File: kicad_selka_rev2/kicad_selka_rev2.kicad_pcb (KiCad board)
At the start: 2 copper layers, 89.2 x 194.1 mm, 88 parts, among them J1 Conn_01x02, J2 Conn_01x06, J3 Conn_01x08, J4 Conn_01x08, SW1 PUSH, U1 ATtiny861A SOIC20

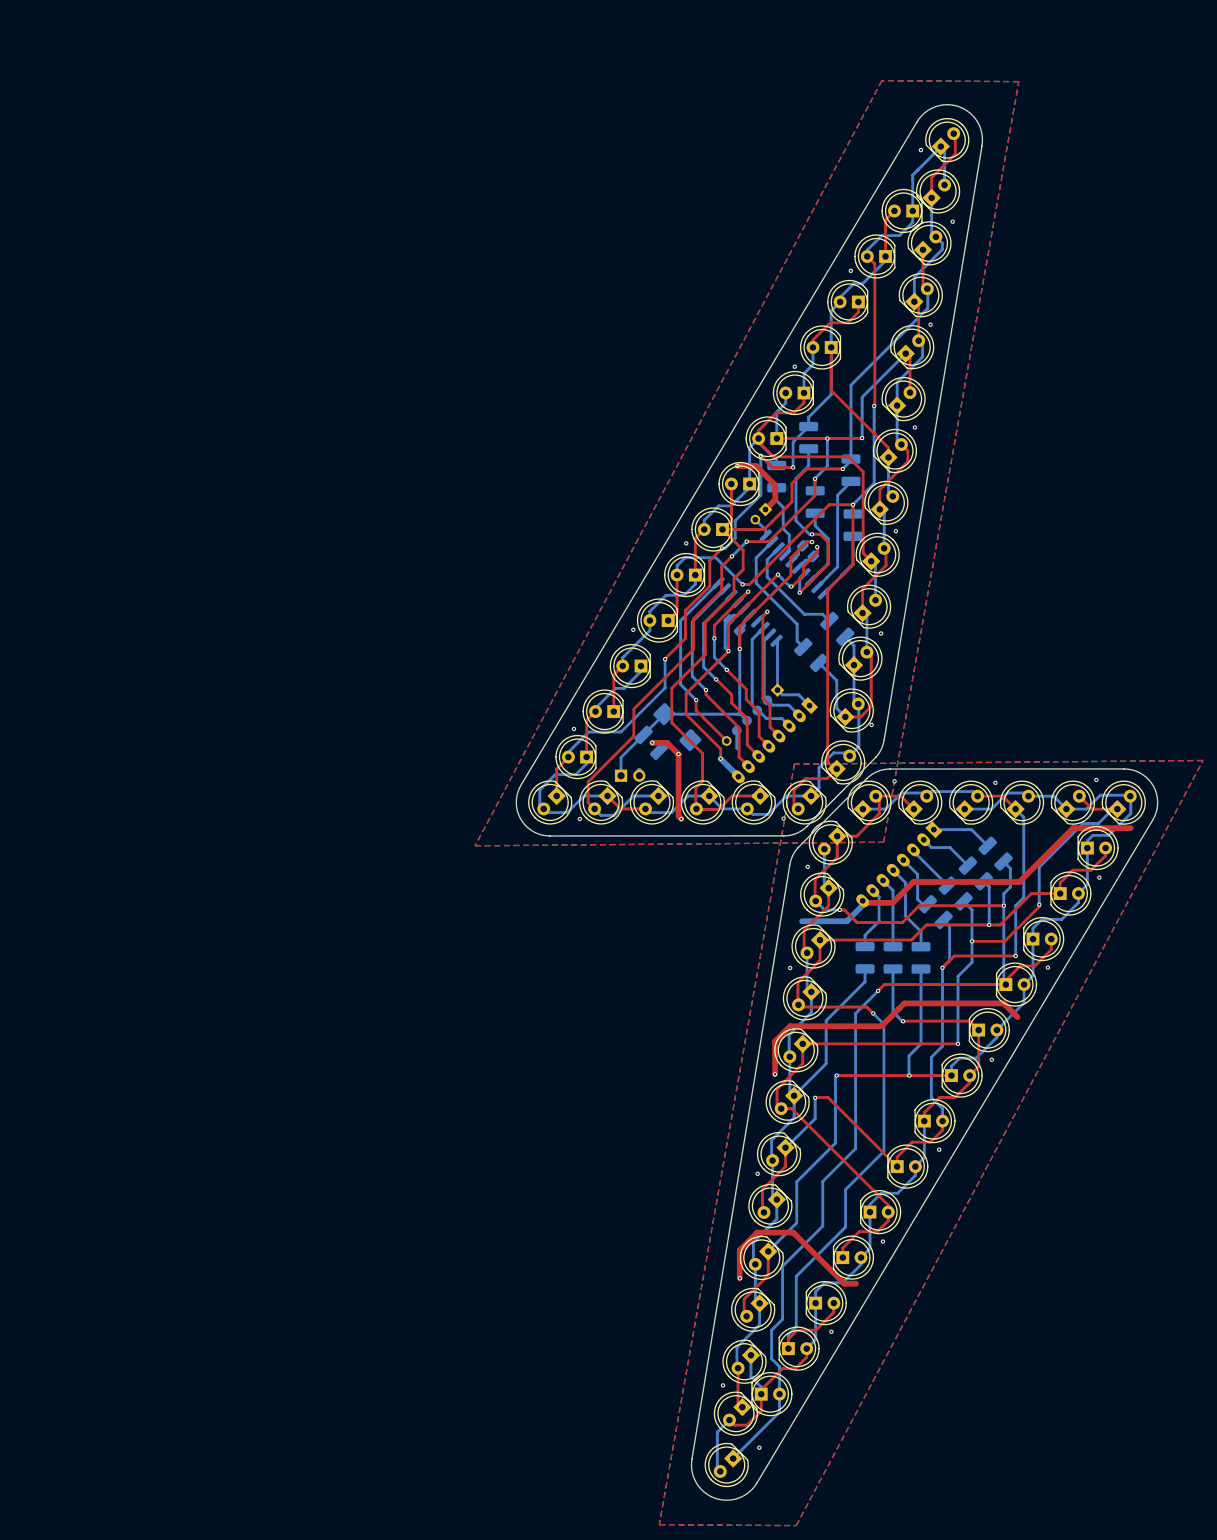
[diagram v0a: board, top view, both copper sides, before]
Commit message: Selkäsalama rev2 done
Skema ja leiska valmis rev2.
Tilattu R2-260625. Toimii ja näyttää hjuvalta.

Siirtin kamaa /archive kansioon. mm. vanhat ja proto versiot.
Vanhat media tiedostot jne.
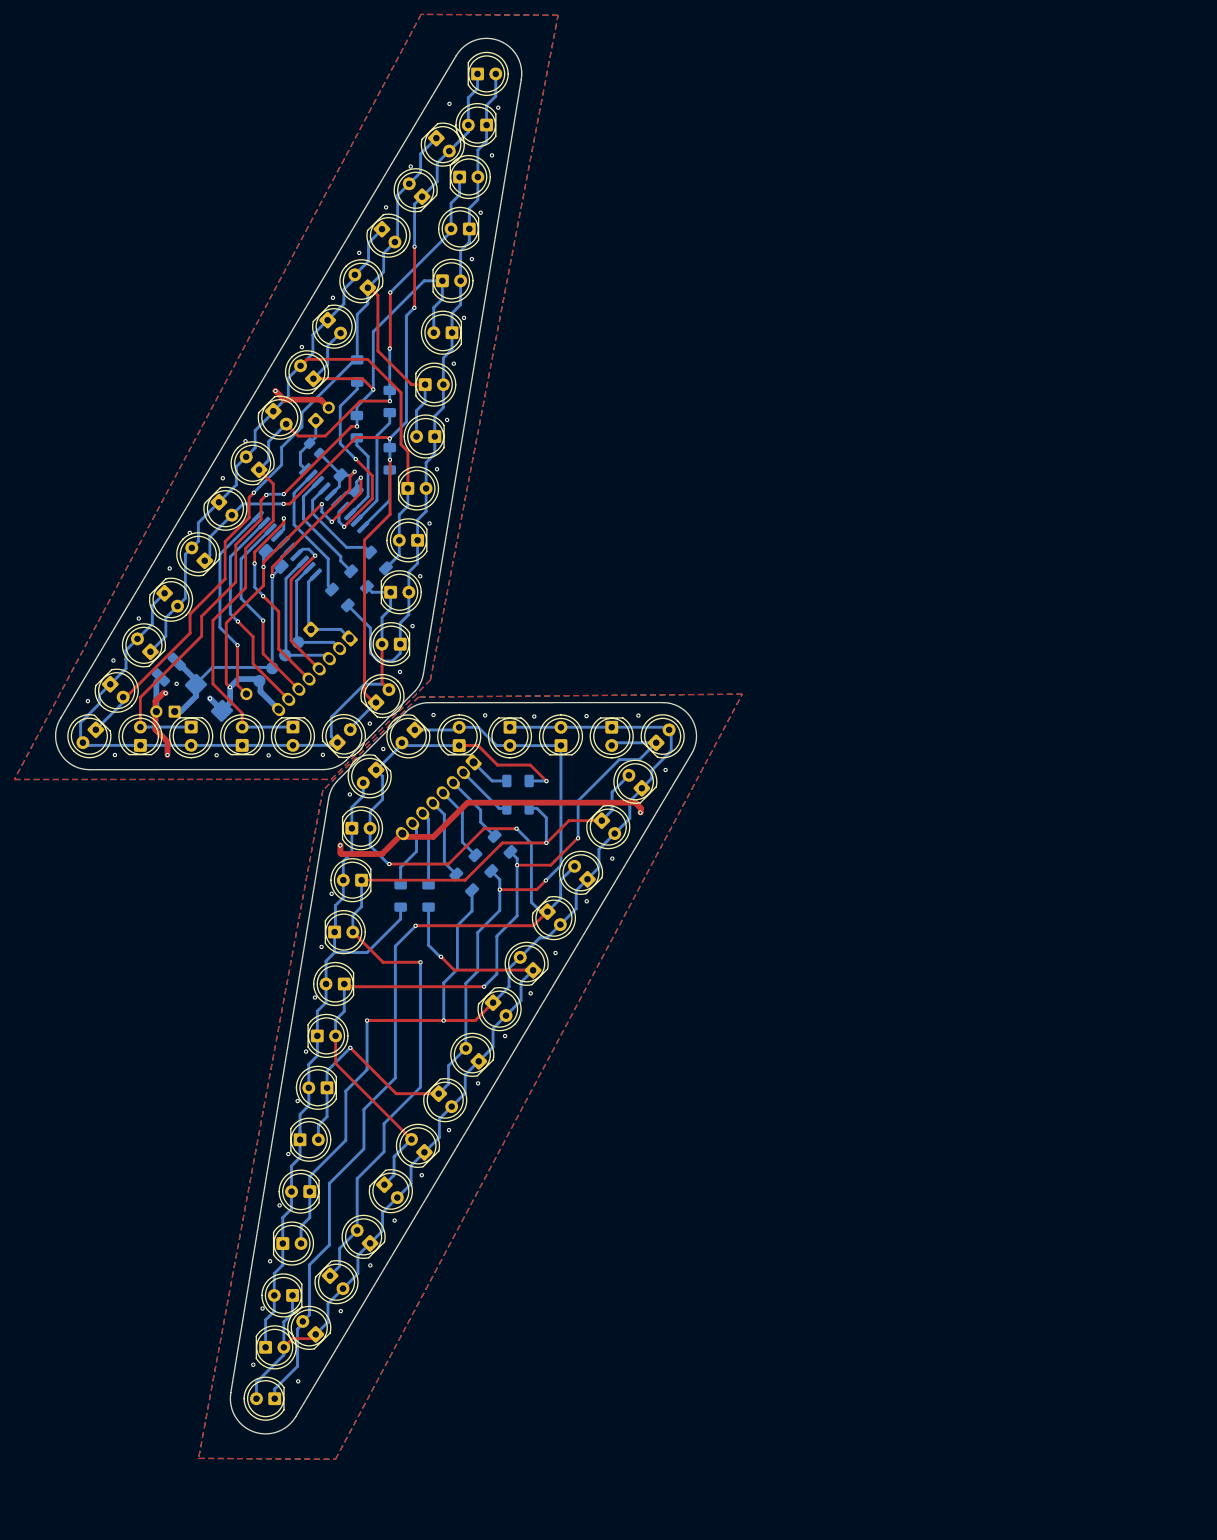
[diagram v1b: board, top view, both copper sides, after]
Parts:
- added G***: LOGO, footprintteja:pesu, B.Cu at (68.7, 162.2)
- added G***: LOGO, footprintteja:avr_logo, B.Cu at (69.1, 64.0)
- added R16: 4.7K, Resistor_SMD:R_0805_2012Metric_Pad1.20x1.40mm_HandSolder, B.Cu at (57.8, 80.9)
- C2, C3: footprint Capacitor_SMD:C_0805_2012Metric_Pad1.18x1.45mm_HandSolder -> Capacitor_SMD:C_1206_3216Metric_Pad1.33x1.80mm_HandSolder
- D1, D10, D11, D12, D13, D14, D15, D16, D17, D18, D19, D2, D20, D21, D22, D23, D24, D25, D26, D27, D28, D29, D3, D30, D31, D32, D33, D34, D35, D36, D37, D38, D39, D4, D40, D41, D42, D43, D44, D45, D46, D47, D48, D49, D5, D50, D51, D52, D53, D54, D55, D56, D57, D58, D59, D6, D60, D61, D62, D63, D64, D7, D8, D9: footprint Library_zani:LED_D5.0mm_blue_zani -> footprintteja:LED_D5.0mm_blue_zani
- J2: footprint footprintteja:PinHeader_1x06_P2.00mm_Horizontal_smd_tht -> footprintteja:PinHeader_1x06_P2.54mm_Horizontal_smd_tht
- R1, R10, R11, R12, R13, R14, R2, R3, R4, R5, R6, R7, R8, R9: value 50 -> 27; footprint Resistor_SMD:R_1210_3225Metric_Pad1.30x2.65mm_HandSolder -> Resistor_SMD:R_1206_3216Metric_Pad1.30x1.75mm_HandSolder
- SW1: value PUSH -> LIUKU; footprint Connector_PinHeader_2.00mm:PinHeader_1x02_P2.00mm_Vertical -> Connector_PinHeader_2.54mm:PinHeader_1x02_P2.54mm_Vertical
- U1: value ATtiny861A SOIC20 -> ATtiny 861A
- moved R15 67.9 mm to (37.5, 111.7), turned to -135 degrees
- moved R8 67.2 mm to (86.1, 127.2), turned to 0 degrees
- moved D52 67.0 mm to (29.4, 113.7), turned to -45 degrees
- moved D58 67.0 mm to (52.1, 75.7), turned to -45 degrees
- moved D60 67.0 mm to (59.6, 63.1), turned to -45 degrees
- moved D54 67.0 mm to (36.9, 101.1), turned to -45 degrees
- moved D56 67.0 mm to (44.5, 88.4), turned to -45 degrees
- moved D62 67.0 mm to (67.2, 50.4), turned to -45 degrees
- moved D64 67.0 mm to (74.7, 37.8), turned to -45 degrees
- moved R6 66.9 mm to (64.0, 99.1)
- moved D15 66.8 mm to (63.0, 133.8), turned to 0 degrees
- moved D19 66.8 mm to (58.2, 162.6), turned to 0 degrees
- moved D25 66.8 mm to (51.0, 206.0), turned to 0 degrees
- moved D17 66.8 mm to (60.6, 148.2), turned to 0 degrees
- moved D21 66.8 mm to (55.8, 177.1), turned to 0 degrees
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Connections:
- D63 pad 1: Net-(D51-K) -> Net-(D1-K)
- D63 pad 2: Net-(D1-K) -> Net-(D51-K)
- D64 pad 1: Net-(D1-K) -> Net-(D51-K)
- D64 pad 2: Net-(D51-K) -> Net-(D1-K)
- SW1 pad 1: GND1 -> Net-(SW1-A)
- SW1 pad 2: Net-(U1-PA7) -> GND1
- U1 pad 11: Net-(U1-PA7) -> Net-(SW1-A)
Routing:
- net GND2: track 117.5 -> 47.1 mm, vias 16 -> 32
- net Net-(D1-K): track 153.1 -> 133.8 mm, vias 3 -> 5
- net Net-(D20-K): track 131.0 -> 112.1 mm
- net Net-(D16-K): track 137.8 -> 119.0 mm
- net Net-(D18-K): track 122.6 -> 109.7 mm
- net Net-(D3-K): track 120.3 -> 109.1 mm, vias 1 -> 3
- net Net-(D14-A): track 108.8 -> 97.9 mm
- net Net-(D51-K): track 134.4 -> 125.6 mm, vias 4 -> 1
- net Net-(SW1-A): track 0.00 -> 7.90 mm
- net Net-(D11-K): track 99.7 -> 92.6 mm
- net +5V: track 60.9 -> 67.7 mm
- net /CA0: track 15.9 -> 9.44 mm
- net Net-(D22-K): track 149.7 -> 143.2 mm
- net Net-(D49-K): track 119.9 -> 114.4 mm, vias 5 -> 4
- net GND1: track 87.8 -> 92.8 mm, vias 23 -> 40
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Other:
- outline, holes or cut-outs redrawn
- board text added: "${SKEMA_REV}-${BOARD_DATE}"
- board text added: "ATtiny 861A"
- board text added: "RES"
- board text removed: "RESET"
- board text removed: "Röh Röh"
